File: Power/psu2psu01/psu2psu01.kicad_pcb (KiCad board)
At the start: 2 copper layers, 142 x 78 mm, 137 parts, among them J1 CONN01PIN, J2 CONN01PIN, J3 CONN01PIN, J4 CONN01PIN, J5 CONN01PIN, J6 CONN01PIN, T1 HM1243, T2 YC13006, T3 HB13006, U1 DM311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

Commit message: up
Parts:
- removed C38: 470x63, mmods:CP4
- removed C41: 0,1, Capacitor_SMD:C_1206_3216Metric
- removed R27: *, ma_misc:RSHUNT1
- removed R53, R54, R55, R56, R57, R58, R59, R60, R61, R62, R63, R64, R65: 10, Resistor_SMD:R_1206_3216Metric
- added R40: 47, mmods:RES2WV01, F.Cu at (128.8, 38.1)
- added R41: 47, mmods:RES2WV01, F.Cu at (128.8, 48.3)
- added R42: 47, mmods:RES2WV01, F.Cu at (128.6, 30.3)
- added R43: ~, Resistor_SMD:R_1206_3216Metric, B.Cu at (136.6, 27.8)
- added R44: ~, Resistor_SMD:R_1206_3216Metric, B.Cu at (141.2, 27.8)
- added R45: ~, Resistor_SMD:R_1206_3216Metric, B.Cu at (141.2, 30.2)
- added R46: ~, Resistor_SMD:R_1206_3216Metric, B.Cu at (136.6, 30.2)
- added R47: ~, Resistor_SMD:R_1206_3216Metric, B.Cu at (141.2, 32.5)
- added R48: ~, Resistor_SMD:R_1206_3216Metric, B.Cu at (141.2, 34.9)
- added R49: ~, Resistor_SMD:R_1206_3216Metric, B.Cu at (136.6, 32.5)
- added R50: ~, Resistor_SMD:R_1206_3216Metric, B.Cu at (136.6, 34.9)
- C25: value 0,01 -> 0,033
- C27, C30: footprint mmods:CP4 -> Capacitor_THT:CP_Radial_D14.0mm_P5.00mm
- C36: footprint Capacitor_SMD:C_1206_3216Metric -> Capacitor_THT:C_Disc_D3.0mm_W2.0mm_P2.50mm
- C37: footprint Capacitor_SMD:C_1206_3216Metric -> Capacitor_THT:C_Disc_D3.0mm_W2.0mm_P2.50mm; moved to F.Cu
- D16, D17: footprint Package_TO_SOT_THT:TO-3P-3_Vertical -> mmods:TO-220-3-01
- R24: value 2k4 -> 1k2
- R25: value 82 -> 75; footprint Capacitor_SMD:C_1206_3216Metric -> Resistor_THT:R_Axial_DIN0207_L6.3mm_D2.5mm_P10.16mm_Horizontal; moved to F.Cu
- R30: value 33k -> 120k*
- R31: value 1k -> 10k
- R33: value 500 -> 5k
- R34: value 4k7 -> 10k
- R38: value 33k -> 47k*
- R51, R52: value 10 -> ~
- moved R51 32.2 mm to (141.2, 37.3)
- moved R39 31.4 mm to (136.6, 77.4), turned to 90 degrees
- moved R38 29.4 mm to (138.6, 81.5), turned to 0 degrees
- moved R52 28.1 mm to (136.6, 37.3), turned to 0 degrees
- moved C37 26.3 mm to (130.1, 41.9), turned to 180 degrees
- moved C39 26.2 mm to (154.5, 49.6)
- moved C28 24.5 mm to (156.7, 66.8), turned to 180 degrees
- moved C36 18.6 mm to (127.6, 52.1), turned to 0 degrees
- moved C31 17.3 mm to (154.4, 63.4)
- moved C40 15.4 mm to (153.4, 35.3), turned to 0 degrees
- moved C30 15.3 mm to (151.9, 53.1)
- moved J6 13.2 mm to (153.0, 75.9)
- moved C27 12.7 mm to (151.9, 38.4)
- moved R25 12.5 mm to (142.7, 64.2)
- moved J5 8.63 mm to (148.0, 45.8)
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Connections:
- C28 pad 2: /GND0 -> GND
- C37 pad 2: Net-(D16-A1) -> Net-(D16-K)
- R51 pad 1: Net-(D16-K) -> /GND0
- R51 pad 2: Net-(C36-Pad2) -> GND
- R52 pad 1: Net-(D16-K) -> /GND0
- R52 pad 2: Net-(C36-Pad2) -> GND
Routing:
- net Net-(C27-Pad1): track 108.6 -> 69.9 mm
- net /GND0: track 150.0 -> 121.2 mm, vias 2 -> 0
- net Net-(D16-K): track 27.4 -> 43.6 mm
- net Net-(R24-Pad2): track 5.65 -> 18.8 mm
- net GND: track 228.9 -> 234.2 mm
- net Net-(U4-FB): track 18.0 -> 22.8 mm
- net Net-(C37-Pad1): track 0.02 -> 4.21 mm
- net Net-(C36-Pad2): track 0.02 -> 4.21 mm
- net Net-(R24-Pad1): track 13.7 -> 9.62 mm
- net Net-(U4-2IN-): track 15.0 -> 18.7 mm
- net Net-(D13-A): track 11.7 -> 8.75 mm
- net Net-(C24-Pad1): track 0.00 -> 2.58 mm
- net Net-(D17-A1): track 24.6 -> 27.1 mm
- net Net-(D16-A1): track 26.9 -> 29.3 mm
- net Net-(R32-Pad1): track 3.86 -> 2.76 mm
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
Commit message: up
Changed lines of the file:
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@@
     (property "ki_description" "Конденсатор полярный")
     (attr through_hole)
-    (fp_text reference "C30" (at 2.5 -8.25) (layer "F.SilkS")
-        (effects (font (size 1 1) (thickness 0.15)))
+    (fp_text reference "C30" (at 8.2 -7.2 90) (layer "F.SilkS")
+        (effects (font (size 1 1) (thickness 0.15) italic))
     )
     (fp_text value "470x63" (at 2.5 8.25) (layer "F.Fab")
@@
     (property "ki_description" "Конденсатор полярный")
     (attr through_hole)
-    (fp_text reference "C27" (at 2.5 -8.25) (layer "F.SilkS")
-        (effects (font (size 1 1) (thickness 0.15)))
+    (fp_text reference "C27" (at 8.5 -6.9 90) (layer "F.SilkS")
+        (effects (font (size 1 1) (thickness 0.15) italic))
     )
     (fp_text value "470x63" (at 2.5 8.25) (layer "F.Fab")

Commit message: up
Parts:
- C11, C12: footprint mmods:CPD11mmW5mmP10mm01 -> mmods:CPD01
- C36: moved to F.Cu
- D13: footprint Diode_SMD:D_1206_3216Metric -> Diode_SMD:D_SMA
- R30: value 120k* -> 100k*
- turned R43 to 180 degrees
- turned R44 to 0 degrees
- turned R45 to 0 degrees
- turned R46 to 180 degrees
- turned R47 to 0 degrees
- turned R48 to 0 degrees
- turned R49 to 180 degrees
- turned R50 to 180 degrees
- turned R51 to 0 degrees
- turned R52 to 180 degrees
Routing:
- net GND1: track 213.0 -> 191.4 mm
- net /+middle: track 79.3 -> 68.7 mm

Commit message: up
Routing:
- net /+middle: track 68.7 -> 50.3 mm
- net /+310: track 122.6 -> 111.2 mm
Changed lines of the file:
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@@
   (segment (start 60.87 70.42) (end 60.6 70.15) (width 1) (layer "B.Cu") (net 12))
   (segment (start 45.05 40.253122) (end 45.05 61.220101) (width 2) (layer "B.Cu") (net 12))
-  (segment (start 47.1 24.7) (end 47.1 35.4) (width 1) (layer "B.Cu") (net 12))
   (segment (start 64.7 72.796015) (end 64.7 80.76) (width 2) (layer "B.Cu") (net 12))
   (segment (start 59.4 70.125) (end 59.4 70.15) (width 2) (layer "B.Cu") (net 12))
@@
   (segment (start 73.3 69.65) (end 71 69.65) (width 2) (layer "B.Cu") (net 12))
   (segment (start 75.822988 70.701245) (end 73.3 69.65) (width 2) (layer "B.Cu") (net 12))
-  (segment (start 47.1 35.4) (end 47.6 35.9) (width 1) (layer "B.Cu") (net 12))
   (segment (start 59.4 70.15) (end 60.6 70.15) (width 2) (layer "B.Cu") (net 12))
   (segment (start 48.828915 34.671084) (end 46.371084 37.128915) (width 2) (layer "B.Cu") (net 12))
@@
   (segment (start 58.2 43.442169) (end 56.8 43.442169) (width 2) (layer "B.Cu") (net 14))
   (segment (start 58.255113 43.497282) (end 58.2 43.442169) (width 2) (layer "B.Cu") (net 14))
-  (segment (start 57.1 24.7) (end 57.1 43.142169) (width 1) (layer "B.Cu") (net 14))
   (segment (start 58.2 41.771084) (end 58.2 43.442169) (width 2) (layer "B.Cu") (net 14))
   (segment (start 56.8 43.442169) (end 52.9 43.442169) (width 2) (layer "B.Cu") (net 14))

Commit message: 30.01up
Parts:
- added R27: 15k, Capacitor_SMD:C_1206_3216Metric, B.Cu at (136.3, 66.8)
- added R53: 33k, Capacitor_SMD:C_1206_3216Metric, B.Cu at (132.2, 65.3)
- added VT5: BC807, Package_TO_SOT_SMD:SOT-23, B.Cu at (131.2, 69.2)
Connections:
- net P4 renamed Net-(U4-DTC)
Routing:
- net Net-(U4-DTC): track 7.23 -> 33.7 mm, vias 1 -> 2
- net Net-(U4-OTC): track 50.4 -> 59.8 mm
- net Net-(C27-Pad1): track 69.9 -> 77.6 mm
- net Net-(VT5-B): track 0.00 -> 6.78 mm
- net SH: track 0.00 -> 2.98 mm, vias 0 -> 1

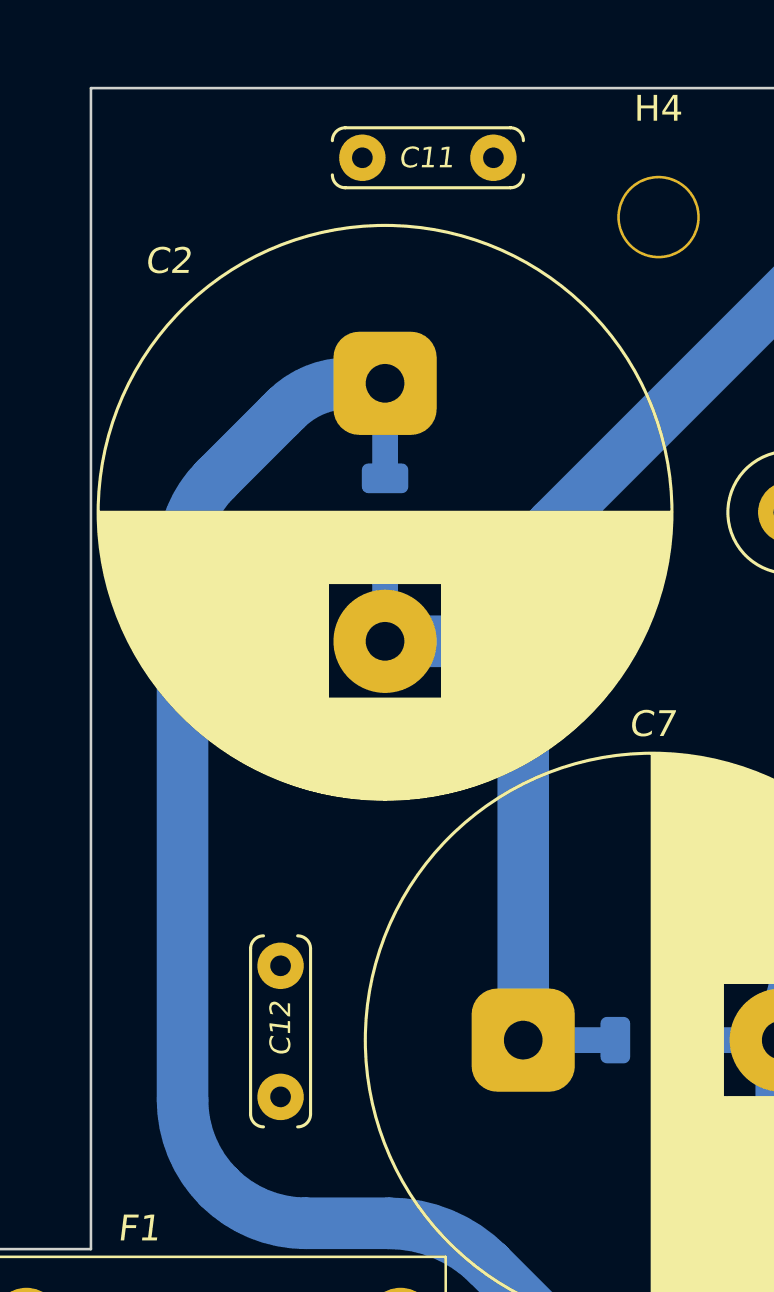
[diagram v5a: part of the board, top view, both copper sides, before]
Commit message: add tyn13butfan
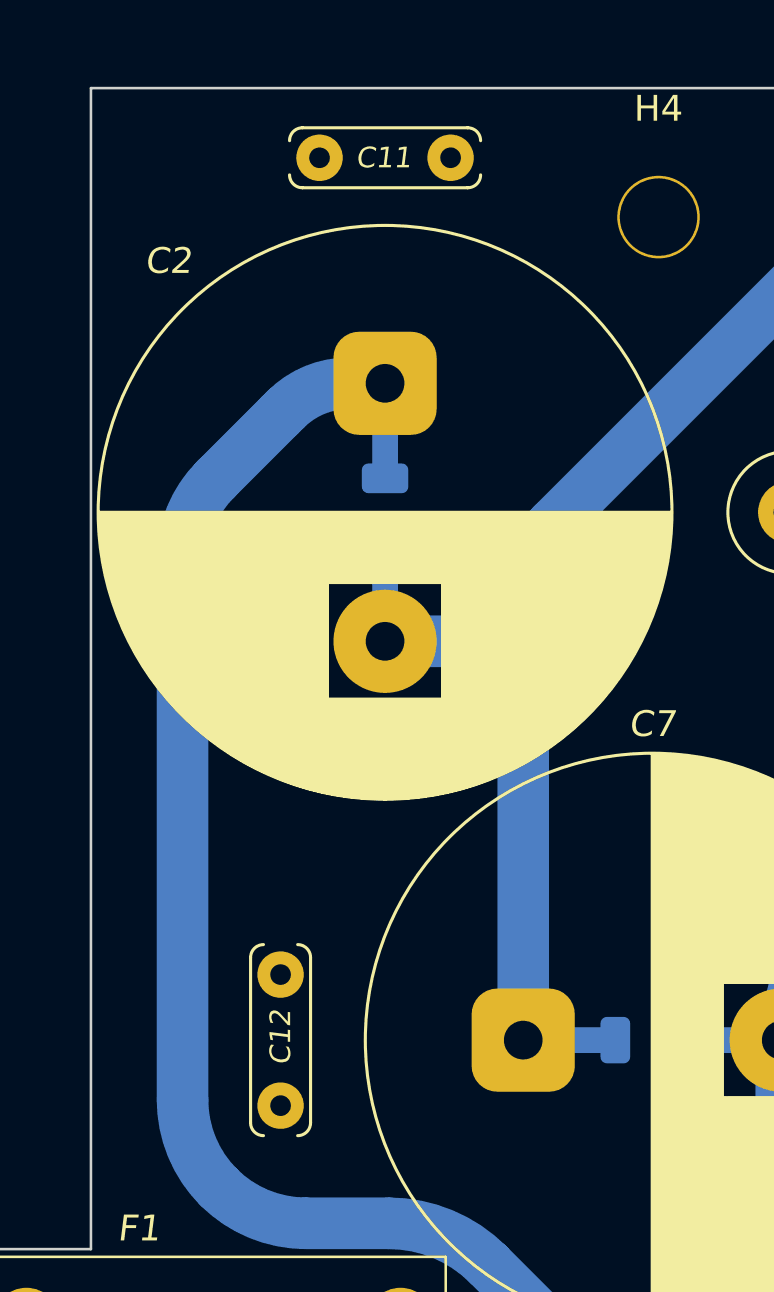
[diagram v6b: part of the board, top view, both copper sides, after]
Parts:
- moved C11 1.66 mm to (55.4, 24.7)
- moved C12 0.34 mm to (48.9, 61.4)
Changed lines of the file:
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@@
   )
   (footprint "mmods:CPD01" (layer "F.Cu")
-    (at 48.85 61.1 90)
+    (at 48.85 61.440001 90)
     (descr "C, Disc series, Radial, pin pitch=10.00mm, , diameter*width=11*5.0mm^2, Capacitor, http://www.vishay.com/docs/28535/vy2series.pdf")
     (tags "C Disc series Radial pin pitch 10.00mm  diameter 11mm width 5.0mm Capacitor")
@@
   )
   (footprint "mmods:CPD01" (layer "F.Cu")
-    (at 57.1 24.7 180)
+    (at 55.440001 24.7 180)
     (descr "C, Disc series, Radial, pin pitch=10.00mm, , diameter*width=11*5.0mm^2, Capacitor, http://www.vishay.com/docs/28535/vy2series.pdf")
     (tags "C Disc series Radial pin pitch 10.00mm  diameter 11mm width 5.0mm Capacitor")

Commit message: up
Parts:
- removed R48, R49, R50, R51, R52: ~, Resistor_SMD:R_1206_3216Metric
- R25: footprint Resistor_THT:R_Axial_DIN0207_L6.3mm_D2.5mm_P10.16mm_Horizontal -> Capacitor_SMD:C_1206_3216Metric; moved to B.Cu
- R42: value 47 -> 3k
- R43, R44, R45: value ~ -> 0,1; footprint Resistor_SMD:R_1206_3216Metric -> Resistor_SMD:R_2512_6332Metric
- R46: value ~ -> 3k; footprint Resistor_SMD:R_1206_3216Metric -> mmods:RES2WV01; moved to F.Cu
- R47: value ~ -> 10k; footprint Resistor_SMD:R_1206_3216Metric -> Potentiometer_THT:Potentiometer_Bourns_3296W_Vertical; moved to F.Cu
- moved R46 30.7 mm to (140.7, 60.6), turned to 0 degrees
- moved R42 30.5 mm to (144.5, 56.3), turned to 180 degrees
- moved R47 29.1 mm to (135.2, 60.9), turned to -90 degrees
- moved J6 9.40 mm to (156.8, 84.5)
- moved C31 9.35 mm to (154.6, 72.8)
- moved C40 7.19 mm to (154.5, 42.4)
- moved R45 3.84 mm to (139.0, 27.1), turned to 90 degrees
- moved R25 3.74 mm to (139.9, 66.7)
- moved C28 2.90 mm to (156.7, 69.7)
- moved R44 2.16 mm to (143.2, 27.1), turned to 90 degrees
- moved R43 1.97 mm to (134.8, 27.1), turned to 90 degrees
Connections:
- H2 pad 1: GND -> unconnected-(H2-Pad1)
- HS2 pad 1: (no net) -> /GND0
- R25 pad 2: /GND0 -> Net-(R25-Pad2)
- R43 pad 1: /GND0 -> GND
- R43 pad 2: GND -> /GND0
- R44 pad 1: /GND0 -> GND
- R44 pad 2: GND -> /GND0
- R45 pad 1: /GND0 -> GND
- R45 pad 2: GND -> /GND0
- R46 pad 1: /GND0 -> Net-(C27-Pad1)
- R46 pad 2: GND -> /GND0
- R47 pad 1: /GND0 -> Net-(R25-Pad2)
- R47 pad 2: GND -> /GND0
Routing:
- net /GND0: track 121.2 -> 155.0 mm
- net Net-(C27-Pad1): track 77.6 -> 104.0 mm, vias 2 -> 4
- net /+middle: track 50.3 -> 73.9 mm
- net GND1: track 191.4 -> 211.2 mm
- net GND: track 234.2 -> 245.9 mm
- net /+310: track 111.2 -> 120.6 mm
- net Net-(R25-Pad2): track 0.00 -> 7.96 mm
- net Net-(R24-Pad2): track 18.8 -> 13.1 mm
- net unconnected-(H2-Pad1): track 0.00 -> 0.72 mm
